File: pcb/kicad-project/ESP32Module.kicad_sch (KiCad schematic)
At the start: 8 parts, among them U1 ESP32-WROOM-32

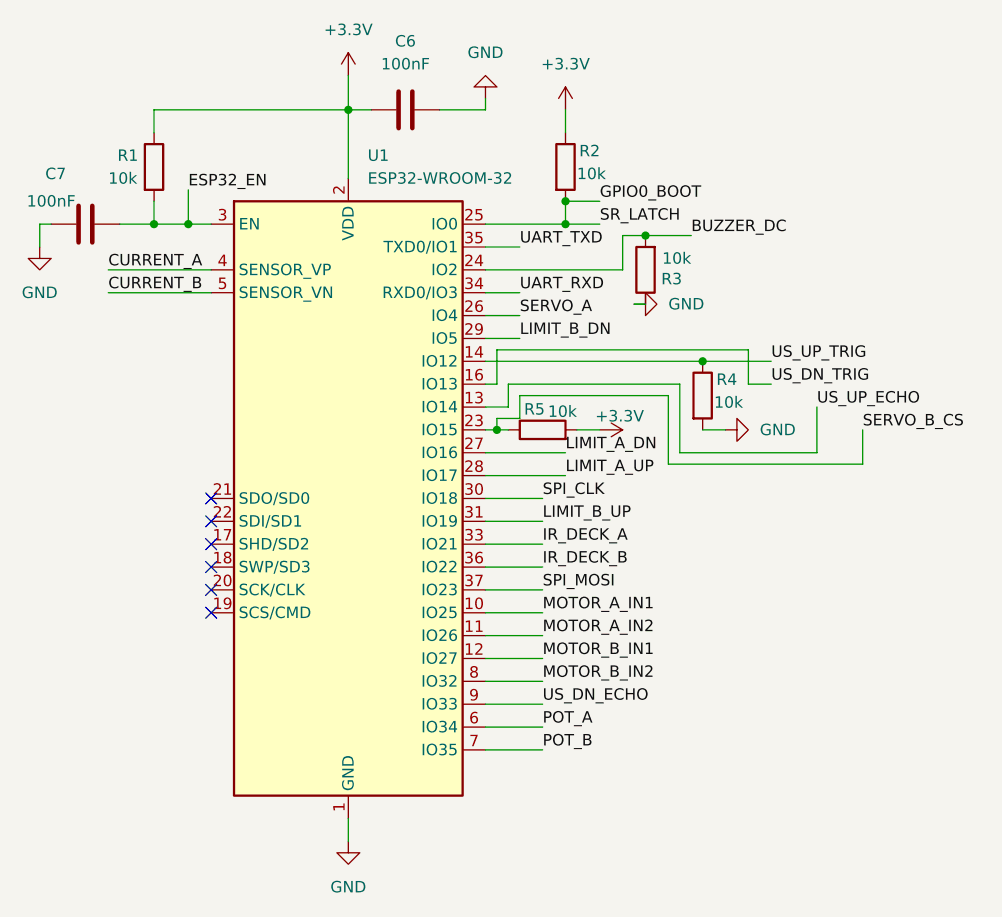
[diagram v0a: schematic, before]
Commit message: Added appropriate footprints to all components in the PCB
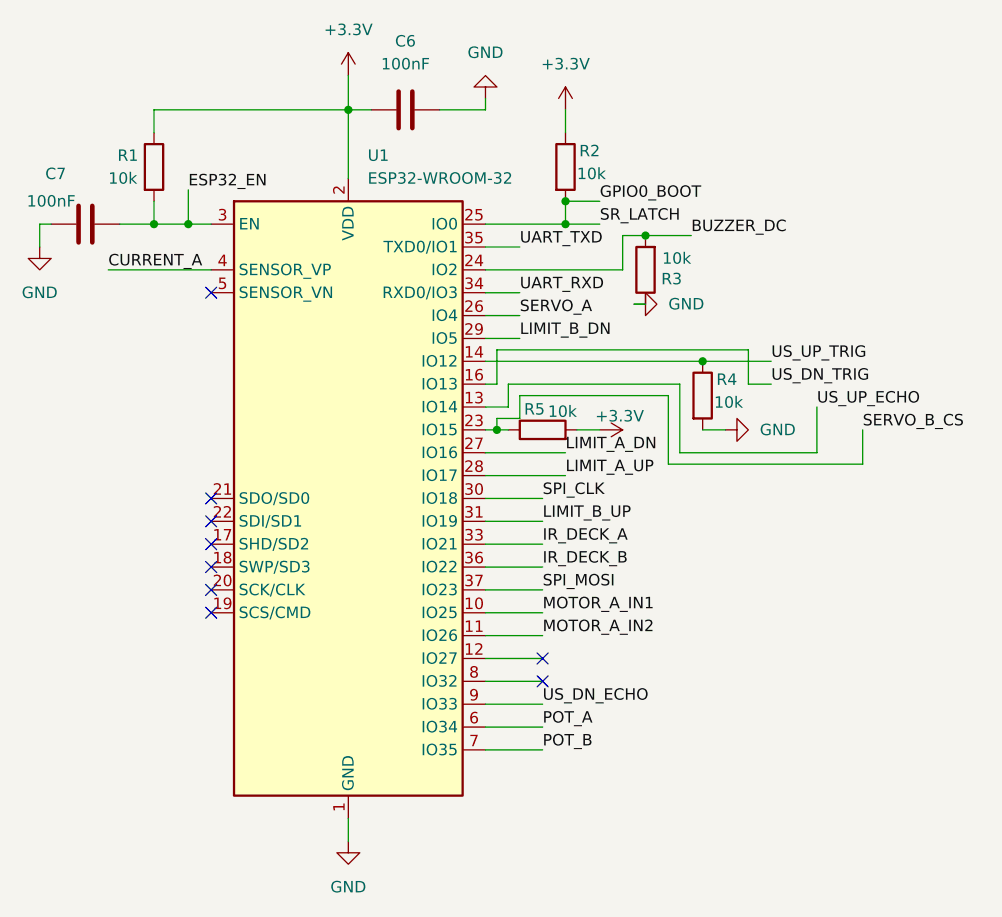
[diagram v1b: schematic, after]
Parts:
- C6, C7: footprint (none) -> Capacitor_SMD:C_0805_2012Metric
- R1, R2, R3, R4, R5: footprint (none) -> Resistor_SMD:R_0805_2012Metric
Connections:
- net CURRENT_B: no longer names the net of U1.5 (SENSOR_VN)
- net MOTOR_B_IN1: no longer names the net of U1.12 (IO27)
- net MOTOR_B_IN2: no longer names the net of U1.8 (IO32)
- no-connect marks 6 -> 9
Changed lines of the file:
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@@
+	)
+	(no_connect
+		(at 128.27 66.04)
+	)
+	(no_connect
+		(at 165.1 109.22)
 	)
 	(no_connect
@@
 	)
 	(no_connect
+		(at 165.1 106.68)
+	)
+	(no_connect
 		(at 128.27 101.6)
 	)
@@
 		(pts
 			(xy 158.75 66.04) (xy 162.56 66.04)
-		)
-		(stroke
-			(width 0)
-			(type default)
-		)
-	)
-	(wire
-		(pts
-			(xy 116.84 66.04) (xy 128.27 66.04)
 		)
 		(stroke
@@
 		)
 	)
-	(label "MOTOR_B_IN1"
-		(at 165.1 106.68 0)
-		(effects
-			(font
-				(size 1.27 1.27)
-			)
-			(justify left bottom)
-		)
-	)
 	(label "US_UP_ECHO"
 		(at 195.58 78.74 0)
@@
 	(label "LIMIT_A_DN"
 		(at 167.64 83.82 0)
-		(effects
-			(font
-				(size 1.27 1.27)
-			)
-			(justify left bottom)
-		)
-	)
-	(label "MOTOR_B_IN2"
-		(at 165.1 109.22 0)
-		(effects
-			(font
-				(size 1.27 1.27)
-			)
-			(justify left bottom)
-		)
-	)
-	(label "CURRENT_B"
-		(at 116.84 66.04 0)
 		(effects
 			(font
@@
 			)
 		)
-		(property "Footprint" ""
+		(property "Footprint" "Resistor_SMD:R_0805_2012Metric"
 			(at 165.862 52.07 90)
 			(effects
@@
 			)
 		)
-		(property "Footprint" ""
+		(property "Footprint" "Capacitor_SMD:C_0805_2012Metric"
 			(at 118.11 57.4548 0)
 			(effects
@@
 			)
 		)
-		(property "Footprint" ""
+		(property "Footprint" "Resistor_SMD:R_0805_2012Metric"
 			(at 178.308 63.5 90)
 			(effects
@@
 			)
 		)
-		(property "Footprint" ""
+		(property "Footprint" "Capacitor_SMD:C_0805_2012Metric"
 			(at 153.67 44.7548 0)
 			(effects
@@
 			)
 		)
-		(property "Footprint" ""
+		(property "Footprint" "Resistor_SMD:R_0805_2012Metric"
 			(at 120.142 52.07 90)
 			(effects
@@
 			)
 		)
-		(property "Footprint" ""
+		(property "Footprint" "Resistor_SMD:R_0805_2012Metric"
 			(at 165.1 83.058 90)
 			(effects
@@
 			)
 		)
-		(property "Footprint" ""
+		(property "Footprint" "Resistor_SMD:R_0805_2012Metric"
 			(at 181.102 77.47 90)
 			(effects
